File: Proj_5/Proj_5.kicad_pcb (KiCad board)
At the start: 2 copper layers, 0 parts

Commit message: Scary
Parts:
- added C1: 0.1uF, Capacitor_Tantalum_SMD:CP_EIA-1608-08_AVX-J, F.Cu at (422.2, -34.2)
- added C10: 0.1uF, Capacitor_Tantalum_SMD:CP_EIA-1608-08_AVX-J, F.Cu at (421.2, 18.3)
- added C11: 0.1uF, Capacitor_Tantalum_SMD:CP_EIA-1608-08_AVX-J, F.Cu at (257.8, 31.6)
- added C12: 0.1uF, Capacitor_Tantalum_SMD:CP_EIA-1608-08_AVX-J, F.Cu at (234.4, 49.9)
- added C13: 0.1uF, Capacitor_Tantalum_SMD:CP_EIA-1608-08_AVX-J, F.Cu at (275.3, 13.3)
- added C14: 0.1uF, Capacitor_Tantalum_SMD:CP_EIA-1608-08_AVX-J, F.Cu at (369.0, 0.80)
- added C15: 0.1uF, Capacitor_Tantalum_SMD:CP_EIA-1608-08_AVX-J, F.Cu at (238.5, 49.9)
- added C16: 0.1uF, Capacitor_Tantalum_SMD:CP_EIA-1608-08_AVX-J, F.Cu at (246.1, 56.0)
- added C17: 0.1uF, Capacitor_Tantalum_SMD:CP_EIA-1608-08_AVX-J, F.Cu at (250.2, 56.0)
- added C18: 0.1uF, Capacitor_Tantalum_SMD:CP_EIA-1608-08_AVX-J, F.Cu at (281.2, 9.00)
- added C19: 0.1uF, Capacitor_Tantalum_SMD:CP_EIA-1608-08_AVX-J, F.Cu at (251.9, 37.9)
- added C2: 0.1uF, Capacitor_Tantalum_SMD:CP_EIA-1608-08_AVX-J, F.Cu at (413.7, 55.5)
- added C20: 0.1uF, Capacitor_Tantalum_SMD:CP_EIA-1608-08_AVX-J, F.Cu at (450.3, 6.23)
- added C21: 100uF, Capacitor_SMD:CP_Elec_3x5.3, F.Cu at (370.3, -2.97)
- added C3: 0.1uF, Capacitor_Tantalum_SMD:CP_EIA-1608-08_AVX-J, F.Cu at (426.3, -36.9)
- added C4: 0.1uF, Capacitor_Tantalum_SMD:CP_EIA-1608-08_AVX-J, F.Cu at (422.2, -36.9)
- added C5: 0.1uF, Capacitor_Tantalum_SMD:CP_EIA-1608-08_AVX-J, F.Cu at (430.4, -36.9)
- added C6: 0.1uF, Capacitor_Tantalum_SMD:CP_EIA-1608-08_AVX-J, F.Cu at (426.3, -34.2)
- added C7: 0.1uF, Capacitor_Tantalum_SMD:CP_EIA-1608-08_AVX-J, F.Cu at (328.8, -21.7)
- added C8: 0.1uF, Capacitor_Tantalum_SMD:CP_EIA-1608-08_AVX-J, F.Cu at (320.6, -21.7)
- added C9: 0.1uF, Capacitor_Tantalum_SMD:CP_EIA-1608-08_AVX-J, F.Cu at (324.7, -21.7)
- added CLK_Gen1: 8284 Clock, Package_DIP:DIP-18_W7.62mm, F.Cu at (442.0, 58.4)
- added CLK_R1: 510 Ohm, Resistor_SMD:R_0201_0603Metric, F.Cu at (422.6, 58.4)
- added CLK_R2: 510 Ohm, Resistor_SMD:R_0201_0603Metric, F.Cu at (427.1, 40.7)
- added D1: LED, LED_THT:LED_D3.0mm_FlatTop, F.Cu at (331.5, 114.3)
- added D2: LED, LED_THT:LED_D3.0mm_FlatTop, F.Cu at (331.5, 121.9)
- added D3: LED, LED_THT:LED_D3.0mm_FlatTop, F.Cu at (331.5, 129.5)
- added D4: LED, LED_THT:LED_D3.0mm_FlatTop, F.Cu at (331.5, 137.2)
- added D5: LED, LED_THT:LED_D3.0mm_FlatTop, F.Cu at (331.5, 144.8)
- added D6: LED, LED_THT:LED_D3.0mm_FlatTop, F.Cu at (331.5, 152.4)
- added D7: LED, LED_THT:LED_D3.0mm_FlatTop, F.Cu at (331.5, 160.0)
- added D8: LED, LED_THT:LED_D3.0mm_FlatTop, F.Cu at (331.5, 167.6)
- added DS1: LCD4x20, parts:LCD4x20, F.Cu at (207.9, -71.4)
- added J1: Conn_02x15_Top_Bottom, Connector_PinHeader_1.00mm:PinHeader_2x15_P1.00mm_Vertical, F.Cu at (605.8, -68.6)
- added J10: Conn_02x20_Counter_Clockwise, Connector_PinHeader_1.00mm:PinHeader_2x20_P1.00mm_Vertical, F.Cu at (342.5, 23.1)
- added J2: Conn_02x15_Top_Bottom, Connector_PinHeader_1.00mm:PinHeader_2x15_P1.00mm_Vertical, F.Cu at (606.1, -26.7)
- added J3: Conn_02x15_Top_Bottom, Connector_PinHeader_1.00mm:PinHeader_2x15_P1.00mm_Vertical, F.Cu at (605.8, -48.3)
- added J4: Conn_02x07_Counter_Clockwise, Connector_PinHeader_1.00mm:PinHeader_2x07_P1.00mm_Vertical, F.Cu at (216.4, 33.3)
- added J5: Conn_02x04_Top_Bottom, Connector_PinHeader_1.00mm:PinHeader_2x04_P1.00mm_Vertical, F.Cu at (253.2, 23.1)
- added J6: Conn_02x06_Counter_Clockwise, Connector_PinHeader_1.00mm:PinHeader_2x06_P1.00mm_Vertical, F.Cu at (346.9, 23.1)
- added J7: DSUB-9, parts:DSUB-9, F.Cu at (453.8, -9.97)
- added J8: Conn_01x02, Connector_PinHeader_1.00mm:PinHeader_1x02_P1.00mm_Vertical, F.Cu at (372.7, 0.98)
- added J9: Conn_02x16_Counter_Clockwise, Connector_PinHeader_1.00mm:PinHeader_2x16_P1.00mm_Vertical, F.Cu at (364.2, -3.87)
- added OSC1: 24 MHz Crystal OSC, Crystal:Crystal_DS10_D1.0mm_L4.3mm_Horizontal, F.Cu at (414.9, 50.8)
- added R1: 10kOhm, Resistor_SMD:R_0402_1005Metric, F.Cu at (292.7, 93.8)
- added R10: 1kOhm, Resistor_SMD:R_0201_0603Metric, F.Cu at (342.9, 121.9)
- added R11: 1kOhm, Resistor_SMD:R_0201_0603Metric, F.Cu at (342.9, 129.5)
- added R12: 1kOhm, Resistor_SMD:R_0201_0603Metric, F.Cu at (342.9, 137.2)
- added R13: 1kOhm, Resistor_SMD:R_0201_0603Metric, F.Cu at (342.9, 144.8)
- added R14: 1kOhm, Resistor_SMD:R_0201_0603Metric, F.Cu at (343.2, 152.4)
- added R15: 1kOhm, Resistor_SMD:R_0201_0603Metric, F.Cu at (342.9, 160.0)
- added R16: 1kOhm, Resistor_SMD:R_0201_0603Metric, F.Cu at (342.9, 167.6)
- added R17: 1kOhm, Resistor_SMD:R_0201_0603Metric, F.Cu at (197.6, 50.3)
- added R19: 1kOhm, Resistor_SMD:R_0201_0603Metric, F.Cu at (235.6, 205.7)
- added R2: 10kOhm, Resistor_SMD:R_0402_1005Metric, F.Cu at (297.2, 93.8)
- added R3: 10kOhm, Resistor_SMD:R_0402_1005Metric, F.Cu at (301.6, 93.8)
- added R4: 10kOhm, Resistor_SMD:R_0402_1005Metric, F.Cu at (306.1, 93.3)
- added R5: 10kOhm, Resistor_SMD:R_0402_1005Metric, F.Cu at (309.9, 93.3)
- added R6: 10kOhm, Resistor_SMD:R_0402_1005Metric, F.Cu at (313.7, 93.3)
- added R7: 10kOhm, Resistor_SMD:R_0402_1005Metric, F.Cu at (321.9, 93.3)
- added R8: 10kOhm, Resistor_SMD:R_0402_1005Metric, F.Cu at (317.5, 93.3)
- added R9: 1kOhm, Resistor_SMD:R_0201_0603Metric, F.Cu at (342.9, 114.3)
- added SW1: SW_DIP_x08, Button_Switch_SMD:SW_DIP_SPSTx08_Slide_Copal_CHS-08A_W5.08mm_P1.27mm_JPin, F.Cu at (280.7, 106.0)
- added SW10: Switch_SW_SPST, Button_Switch_SMD:SW_SPST_B3U-1000P-B, F.Cu at (179.1, 389.3)
- added SW11: Switch_SW_SPST, Button_Switch_SMD:SW_SPST_B3U-1000P-B, F.Cu at (186.7, 389.3)
- added SW12: Switch_SW_SPST, Button_Switch_SMD:SW_SPST_B3U-1000P-B, F.Cu at (156.2, 395.6)
- added SW13: Switch_SW_SPST, Button_Switch_SMD:SW_SPST_B3U-1000P-B, F.Cu at (163.8, 395.6)
- added SW14: Switch_SW_SPST, Button_Switch_SMD:SW_SPST_B3U-1000P-B, F.Cu at (171.4, 395.6)
- added SW15: Switch_SW_SPST, Button_Switch_SMD:SW_SPST_B3U-1000P-B, F.Cu at (179.1, 395.6)
- added SW16: Switch_SW_SPST, Button_Switch_SMD:SW_SPST_B3U-1000P-B, F.Cu at (186.7, 395.6)
- added SW17: Switch_SW_SPST, Button_Switch_SMD:SW_SPST_B3U-1000P-B, F.Cu at (156.2, 402.0)
- added SW18: Switch_SW_SPST, Button_Switch_SMD:SW_SPST_B3U-1000P-B, F.Cu at (163.8, 402.0)
- added SW19: Switch_SW_SPST, Button_Switch_SMD:SW_SPST_B3U-1000P-B, F.Cu at (171.4, 402.0)
- added SW2: Shift, Button_Switch_SMD:SW_SPST_B3U-1000P-B, F.Cu at (156.2, 382.9)
- added SW20: Switch_SW_SPST, Button_Switch_SMD:SW_SPST_B3U-1000P-B, F.Cu at (179.1, 402.0)
- added SW21: Switch_SW_SPST, Button_Switch_SMD:SW_SPST_B3U-1000P-B, F.Cu at (186.7, 402.0)
- added SW22: Switch_SW_SPST, Button_Switch_SMD:SW_SPST_B3U-1000P-B, F.Cu at (156.2, 408.3)
- added SW23: Switch_SW_SPST, Button_Switch_SMD:SW_SPST_B3U-1000P-B, F.Cu at (163.8, 408.3)
- added SW24: NMI Button, Button_Switch_SMD:SW_SPST_B3U-1000P-B, F.Cu at (171.4, 408.3)
- added SW25: Reset Button, Button_Switch_SMD:SW_SPST_B3U-1000P-B, F.Cu at (179.1, 408.3)
- added SW26: IR0 Button, Button_Switch_SMD:SW_SPST_B3U-1000P-B, F.Cu at (186.7, 408.3)
- added SW3: Switch_SW_SPST, Button_Switch_SMD:SW_SPST_B3U-1000P-B, F.Cu at (163.8, 382.9)
- added SW4: Switch_SW_SPST, Button_Switch_SMD:SW_SPST_B3U-1000P-B, F.Cu at (171.4, 382.9)
- added SW5: Switch_SW_SPST, Button_Switch_SMD:SW_SPST_B3U-1000P-B, F.Cu at (179.1, 382.9)
- added SW6: Switch_SW_SPST, Button_Switch_SMD:SW_SPST_B3U-1000P-B, F.Cu at (186.7, 382.9)
- added SW7: CTRL, Button_Switch_SMD:SW_SPST_B3U-1000P-B, F.Cu at (156.2, 389.3)
- added SW8: Switch_SW_SPST, Button_Switch_SMD:SW_SPST_B3U-1000P-B, F.Cu at (163.8, 389.3)
- added SW9: Switch_SW_SPST, Button_Switch_SMD:SW_SPST_B3U-1000P-B, F.Cu at (171.4, 389.3)
- added U1: 8255, Package_DIP:DIP-40_W15.24mm, F.Cu at (569.0, -68.6)
- added U10: 8259, Package_DIP:DIP-28_W15.24mm, F.Cu at (216.3, -3.32)
- added U11: 8254, Package_DIP:DIP-24_W15.24mm, F.Cu at (234.7, -3.32)
- added U12: 28F010, parts:28F010, F.Cu at (197.9, 57.4)
- added U13: PAL16L8, Package_DIP:DIP-20_W7.62mm, F.Cu at (624.8, 162.6)
- added U14: 16550, Package_DIP:DIP-40_W15.24mm, F.Cu at (511.8, 22.9)
- added U15: PAL16L8, Package_DIP:DIP-20_W7.62mm, F.Cu at (561.3, 162.6)
- added U16: PAL16L8, Package_DIP:DIP-20_W7.62mm, F.Cu at (623.6, 128.3)
- added U17: pkd8279, parts:pkd8279, F.Cu at (105.4, 429.9)
- added U18: 74LS138, Package_DIP:DIP-16_W7.62mm, F.Cu at (234.8, 28.8)
- added U19: 8086_Min_Mode, Package_DIP:DIP-40_W15.24mm, F.Cu at (302.3, -3.32)
- added U2: 8255, Package_DIP:DIP-40_W15.24mm, F.Cu at (569.0, -7.62)
- added U20: 74LS373, Package_DIP:DIP-20_W7.62mm, F.Cu at (331.6, 23.7)
- added U21: 74LS373, Package_DIP:DIP-20_W7.62mm, F.Cu at (320.8, 23.7)
- added U22: 74LS244, Package_DIP:DIP-20_W7.62mm, F.Cu at (353.3, -3.32)
- added U23: 74LS373, Package_DIP:DIP-20_W7.62mm, F.Cu at (342.5, -3.32)
- added U24: 74LS245, Package_DIP:DIP-20_W7.62mm, F.Cu at (331.6, -3.32)
- added U25: 74LS245, Package_DIP:DIP-20_W7.62mm, F.Cu at (320.8, -3.32)
- added U3: 8255, Package_DIP:DIP-40_W15.24mm, F.Cu at (569.0, 54.6)
- added U33: 74LS374, Package_DIP:DIP-20_W7.62mm, F.Cu at (302.4, 54.3)
- added U34: MAN72A, Display_7Segment:MAN72A, F.Cu at (208.9, 205.7)
- added U35: PAL16L8, Package_DIP:DIP-20_W7.62mm, F.Cu at (28.4, 392.9)
- added U36: 74LS374, Package_DIP:DIP-20_W7.62mm, F.Cu at (313.2, 54.3)
- added U37: MAN72A, Display_7Segment:MAN72A, F.Cu at (208.9, 231.1)
- added U38: PAL16L8, Package_DIP:DIP-20_W7.62mm, F.Cu at (28.6, 362.6)
- added U39: PAL16L8, Package_DIP:DIP-20_W7.62mm, F.Cu at (599.4, 128.3)
- added U4: 28F010, parts:28F010, F.Cu at (216.4, 57.4)
- added U40: PAL16L8, Package_DIP:DIP-20_W7.62mm, F.Cu at (595.6, 162.6)
- added U48: MAX6816, Package_TO_SOT_SMD:SOT-143, F.Cu at (246.6, 42.0)
- added U49: MAX6816, Package_TO_SOT_SMD:SOT-143, F.Cu at (287.5, 1.23)
- added U5: CY7C199, Package_DIP:DIP-28_W15.24mm, F.Cu at (421.7, -73.4)
- added U50: MAX6816, Package_TO_SOT_SMD:SOT-143, F.Cu at (252.4, 34.3)
- added U51: PAL16L8, Package_DIP:DIP-20_W7.62mm, F.Cu at (570.2, 128.3)
- added U52: PAL16L8, Package_DIP:DIP-20_W7.62mm, F.Cu at (546.1, 128.3)
- added U55: max235cpg, parts:max235cpg, F.Cu at (435.9, 14.0)
- added U56: 74LS374, Package_DIP:DIP-20_W7.62mm, F.Cu at (389.3, 125.1)
- added U57: 74LS244, Package_DIP:DIP-20_W7.62mm, F.Cu at (345.8, 54.3)
- added U59: PAL16L8, Package_DIP:DIP-20_W7.62mm, F.Cu at (334.9, 54.3)
- added U6: CY7C199, Package_DIP:DIP-28_W15.24mm, F.Cu at (440.1, -73.4)
- added U61: PAL16L8, Package_DIP:DIP-20_W7.62mm, F.Cu at (324.1, 54.3)
- added U7: PAL16L8, Package_DIP:DIP-20_W7.62mm, F.Cu at (524.5, 128.3)
- added U8: CY7C199, Package_DIP:DIP-28_W15.24mm, F.Cu at (476.9, -73.4)
- added U9: CY7C199, Package_DIP:DIP-28_W15.24mm, F.Cu at (458.5, -73.4)

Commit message: Playing with PCB placements
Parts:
- added C22: 0.1uF, Capacitor_Tantalum_SMD:CP_EIA-1608-08_AVX-J, F.Cu at (200.7, 262.9)
- moved U35 574.3 mm to (588.4, 265.9)
- moved U38 574.3 mm to (588.6, 235.6)
- moved J4 473.1 mm to (25.4, 466.1)
- moved U11 471.8 mm to (90.2, 445.8)
- moved U18 431.8 mm to (149.9, 452.1), turned to 90 degrees
- moved R17 409.6 mm to (162.6, 458.5), turned to 270 degrees
- moved U57 404.8 mm to (307.3, 457.2)
- moved U36 386.1 mm to (443.2, 417.8), turned to 90 degrees
- moved J5 385.9 mm to (31.8, 339.1)
- moved U49 378.0 mm to (189.3, 366.3), turned to 270 degrees
- moved U33 376.1 mm to (398.8, 417.8), turned to 90 degrees
- moved C18 367.2 mm to (194.3, 365.8), turned to 90 degrees
- moved R1 362.1 mm to (261.0, 454.5)
- moved R2 362.1 mm to (265.4, 454.5)
- moved R3 362.1 mm to (269.9, 454.5)
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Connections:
- J4 pad 10: GND -> Net-(J4-Pad10)
- J4 pad 11: GND -> Net-(J4-Pad11)
- J4 pad 12: GND -> Net-(J4-Pad12)
- J4 pad 13: GND -> Net-(J4-Pad13)
- J4 pad 14: GND -> Net-(J4-Pad14)
- J4 pad 9: GND -> Net-(J4-Pad9)

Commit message: Hey Collin
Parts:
- moved C12 336.1 mm to (71.8, 344.1), turned to 90 degrees
- moved C16 188.7 mm to (363.3, 203.8), turned to 180 degrees
- moved C17 149.4 mm to (363.2, 153.7), turned to 180 degrees
- moved U35 137.2 mm to (654.0, 145.4)
- moved U38 118.1 mm to (664.9, 145.4)
- moved U11 55.2 mm to (36.2, 457.2)
- moved U4 53.0 mm to (355.6, 161.3)
- moved U10 40.0 mm to (52.7, 345.4)
- moved J5 32.0 mm to (63.7, 336.6), turned to 90 degrees
- moved C22 18.5 mm to (202.6, 244.5)
- moved U17 10.9 mm to (104.1, 440.7)
- moved U24 0.64 mm to (201.9, 136.5)
- moved U12 0.45 mm to (355.6, 211.5)
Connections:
- U10 pad 22: Net-(J5-Pad4) -> Net-(J5-Pad1)
- U10 pad 24: Net-(J5-Pad2) -> Net-(J5-Pad5)
- U10 pad 25: Net-(J5-Pad1) -> Net-(J5-Pad7)
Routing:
- net /A1: track 0.00 -> 95.4 mm, vias 0 -> 1
- net /A2: track 0.00 -> 95.1 mm, vias 0 -> 1
- net /A3: track 0.00 -> 94.7 mm, vias 0 -> 1
- net /A4: track 0.00 -> 94.6 mm, vias 0 -> 1
- net /A7: track 0.00 -> 94.3 mm, vias 0 -> 1
- net /A6: track 0.00 -> 94.3 mm, vias 0 -> 1
- net /A5: track 0.00 -> 94.3 mm, vias 0 -> 1
- net /A0: track 0.00 -> 51.9 mm
- net /D0: track 0.00 -> 51.5 mm
- net /D1: track 0.00 -> 48.9 mm
- net /8279, 8259, 8254/INT: track 0.00 -> 47.4 mm
- net /D2: track 0.00 -> 46.1 mm
- net /D3: track 0.00 -> 43.3 mm
- net /D4: track 0.00 -> 40.5 mm
- net /D5: track 0.00 -> 37.7 mm
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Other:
- board outline added: 717.5 x 762 mm
- copper layers 2 -> 4

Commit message: Cool stuff
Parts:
- moved C16 66.5 mm to (378.5, 139.1)
- moved U12 66.5 mm to (370.8, 146.7)
- moved U4 66.5 mm to (370.8, 96.5)
- moved C17 66.5 mm to (378.5, 88.9)
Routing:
- net /A14: track 16.5 -> 276.0 mm, vias 0 -> 2
- net /A13: track 16.5 -> 272.4 mm, vias 0 -> 2
- net /A11: track 16.5 -> 264.3 mm, vias 0 -> 2
- net /A8: track 16.5 -> 264.1 mm, vias 0 -> 2
- net /A9: track 16.5 -> 263.4 mm, vias 0 -> 2
- net /A10: track 16.5 -> 262.2 mm, vias 0 -> 2
- net /A16: track 0.00 -> 184.4 mm, vias 0 -> 2
- net /A15: track 0.00 -> 183.0 mm, vias 0 -> 2
- net /A12: track 0.00 -> 179.4 mm, vias 0 -> 2
- net /~WR: track 18.2 -> 187.2 mm, vias 0 -> 3
- net /~RD: track 21.0 -> 165.6 mm, vias 0 -> 2
- net /D8: track 0.00 -> 122.9 mm, vias 0 -> 2
- net /D9: track 0.00 -> 118.7 mm, vias 0 -> 2
- net /D10: track 0.00 -> 115.2 mm, vias 0 -> 2
- net /~BHE: track 0.00 -> 103.4 mm, vias 0 -> 1
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
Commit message: Bus time
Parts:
- moved U6 410.2 mm to (412.1, 335.9)
- moved U5 372.2 mm to (412.2, 298.8)
- moved C6 372.1 mm to (289.6, 311.8)
- moved C5 372.0 mm to (289.5, 307.3)
- moved C3 366.3 mm to (289.6, 302.9)
- moved C1 358.1 mm to (289.6, 298.4)
- moved C4 356.5 mm to (289.6, 294.0)
- moved U9 337.5 mm to (412.1, 261.0)
- moved U8 304.2 mm to (412.1, 223.8)
- moved R19 34.9 mm to (459.7, 382.9)
- moved U34 10.8 mm to (419.1, 385.4)
- moved U37 10.8 mm to (435.6, 385.4)
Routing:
- net /A14: track 276.0 -> 498.8 mm
- net /A13: track 272.4 -> 487.3 mm, vias 2 -> 8
- net /A12: track 179.4 -> 386.5 mm, vias 2 -> 8
- net /A11: track 264.3 -> 463.5 mm, vias 2 -> 8
- net /A10: track 262.2 -> 453.5 mm, vias 2 -> 8
- net /A1: track 157.7 -> 343.5 mm, vias 2 -> 8
- net /A9: track 263.4 -> 446.8 mm, vias 2 -> 8
- net /A2: track 159.8 -> 337.4 mm, vias 2 -> 8
- net /A8: track 264.1 -> 439.6 mm, vias 2 -> 8
- net /A3: track 162.0 -> 333.0 mm, vias 2 -> 8
- net /A7: track 171.8 -> 339.5 mm, vias 2 -> 8
- net /~RD: track 165.6 -> 330.0 mm, vias 2 -> 6
- net /A4: track 164.4 -> 328.8 mm, vias 2 -> 8
- net /A6: track 169.3 -> 329.0 mm, vias 2 -> 8
- net /A5: track 166.7 -> 318.2 mm, vias 2 -> 8
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
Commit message: Keyboard + Individual LEDS
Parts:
- moved C5 94.5 mm to (208.2, 259.1)
- moved C6 94.5 mm to (208.3, 263.5)
- moved C1 94.5 mm to (208.4, 250.2)
- moved C3 94.5 mm to (208.4, 254.6)
- moved C4 94.5 mm to (208.3, 245.7)
- moved U23 89.2 mm to (191.8, 177.8), turned to 270 degrees
- moved U21 87.7 mm to (135.9, 179.1), turned to 270 degrees
- moved DS1 84.5 mm to (143.5, 292.1)
- moved C22 84.5 mm to (140.4, 301.6)
- moved U20 80.7 mm to (213.4, 29.2)
- moved U25 49.4 mm to (223.5, 139.7)
- moved U24 42.1 mm to (223.5, 100.3)
- moved U56 25.3 mm to (299.1, 365.1)
- moved C15 19.2 mm to (162.6, 368.3), turned to 270 degrees
- moved C18 15.5 mm to (179.1, 368.3), turned to 270 degrees
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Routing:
- net Net-(SW11-Pad1): track 0.00 -> 151.2 mm, vias 0 -> 6
- net Net-(SW10-Pad1): track 0.00 -> 150.9 mm, vias 0 -> 6
- net Net-(SW20-Pad2): track 3.33 -> 135.0 mm
- net Net-(SW13-Pad1): track 0.00 -> 129.5 mm, vias 0 -> 6
- net Net-(SW12-Pad1): track 0.00 -> 128.3 mm, vias 0 -> 5
- net Net-(SW16-Pad2): track 1.10 -> 126.0 mm
- net Net-(SW12-Pad2): track 2.20 -> 120.6 mm
- net Net-(SW10-Pad2): track 1.10 -> 102.0 mm
- net Net-(U17-Pad34): track 0.00 -> 91.0 mm
- net Net-(SW2-Pad2): track 1.80 -> 92.7 mm
- net Net-(U17-Pad32): track 0.00 -> 90.5 mm, vias 0 -> 1
- net Net-(U17-Pad33): track 0.00 -> 89.8 mm, vias 0 -> 1
- net Net-(R16-Pad2): track 0.00 -> 78.0 mm, vias 0 -> 1
- net Net-(SW7-Pad1): track 0.00 -> 77.9 mm, vias 0 -> 1
- net Net-(R15-Pad2): track 0.00 -> 70.8 mm, vias 0 -> 1
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
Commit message: Complete Data Bus
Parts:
- moved U25 291.8 mm to (199.4, -151.1)
- moved U24 287.1 mm to (228.6, -186.7)
- moved U19 281.7 mm to (61.0, -129.5)
- moved U21 271.7 mm to (99.1, -90.2)
- moved U23 263.3 mm to (177.8, -85.1)
- moved U55 180.1 mm to (553.7, -209.6)
- moved U14 169.4 mm to (510.5, -143.5)
- moved U7 145.5 mm to (604.5, -133.3)
- moved J7 88.5 mm to (391.2, -247.7)
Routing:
- net Net-(U19-Pad16): track 3.07 -> 188.7 mm, vias 0 -> 2
- net Net-(U19-Pad9): track 3.07 -> 181.8 mm
- net Net-(U19-Pad10): track 3.07 -> 180.8 mm, vias 0 -> 2
- net Net-(U19-Pad11): track 3.07 -> 177.6 mm, vias 0 -> 2
- net Net-(U19-Pad12): track 3.07 -> 175.5 mm, vias 0 -> 2
- net Net-(U19-Pad13): track 3.07 -> 173.4 mm, vias 0 -> 2
- net Net-(U19-Pad15): track 3.07 -> 172.4 mm, vias 0 -> 2
- net Net-(U19-Pad14): track 3.07 -> 171.3 mm, vias 0 -> 2
- net Net-(U19-Pad8): track 3.07 -> 164.2 mm, vias 0 -> 2
- net Net-(U19-Pad39): track 18.8 -> 162.6 mm
- net Net-(U19-Pad2): track 3.07 -> 146.3 mm, vias 0 -> 2
- net Net-(U19-Pad7): track 3.07 -> 145.4 mm, vias 0 -> 2
- net Net-(U19-Pad3): track 3.07 -> 144.2 mm, vias 0 -> 2
- net Net-(U19-Pad4): track 3.07 -> 143.9 mm, vias 0 -> 2
- net Net-(U19-Pad5): track 3.07 -> 143.6 mm, vias 0 -> 2
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
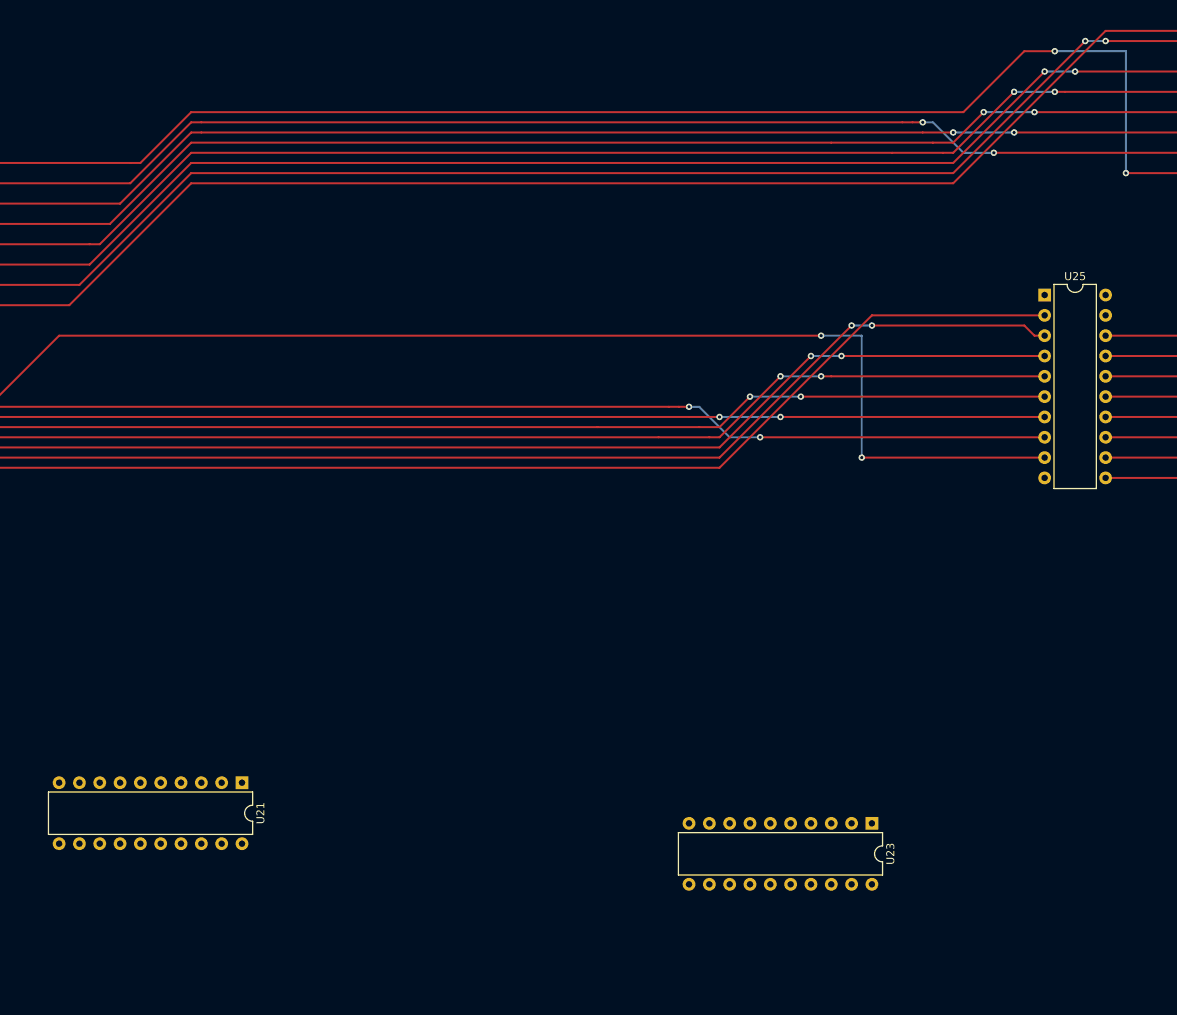
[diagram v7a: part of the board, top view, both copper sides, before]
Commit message: Addresses 8-15
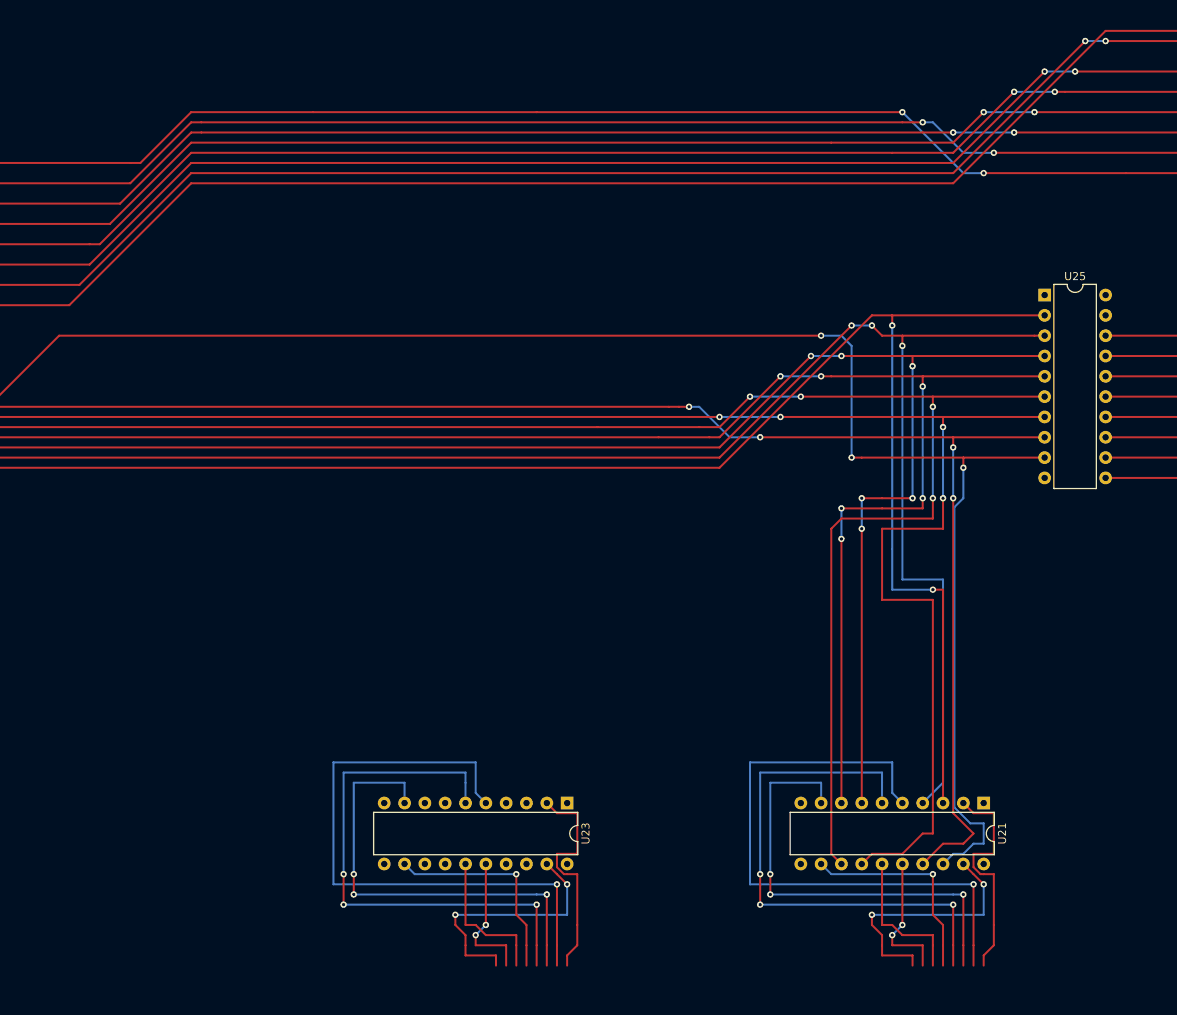
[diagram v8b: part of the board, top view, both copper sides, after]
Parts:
- moved U21 92.7 mm to (191.8, -87.6)
- moved U23 38.2 mm to (139.7, -87.6)
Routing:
- net /A6: track 329.0 -> 405.8 mm, vias 8 -> 9
- net /A14: track 498.8 -> 575.5 mm, vias 2 -> 3
- net Net-(U19-Pad6): track 142.5 -> 219.1 mm, vias 2 -> 4
- net Net-(U19-Pad5): track 143.6 -> 214.5 mm, vias 2 -> 4
- net /A13: track 487.3 -> 554.6 mm, vias 8 -> 11
- net Net-(U19-Pad39): track 162.6 -> 229.9 mm, vias 0 -> 2
- net /A5: track 318.2 -> 385.5 mm, vias 8 -> 11
- net Net-(U19-Pad2): track 146.3 -> 210.9 mm, vias 2 -> 3
- net Net-(U19-Pad4): track 143.9 -> 207.4 mm, vias 2 -> 6
- net Net-(U19-Pad3): track 144.2 -> 206.4 mm, vias 2 -> 6
- net Net-(U19-Pad7): track 145.4 -> 203.9 mm, vias 2 -> 4
- net Net-(U19-Pad8): track 164.2 -> 220.8 mm, vias 2 -> 3
- net /A4: track 328.8 -> 384.7 mm, vias 8 -> 11
- net /A12: track 386.5 -> 442.4 mm, vias 8 -> 11
- net /A8: track 439.6 -> 471.7 mm, vias 8 -> 10
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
